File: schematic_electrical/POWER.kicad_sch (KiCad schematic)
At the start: 5 parts, among them SW1 WGCD_SPST_ILLUM_TOGGLE, SW2 WGCD_SPST_ILLUM_TOGGLE

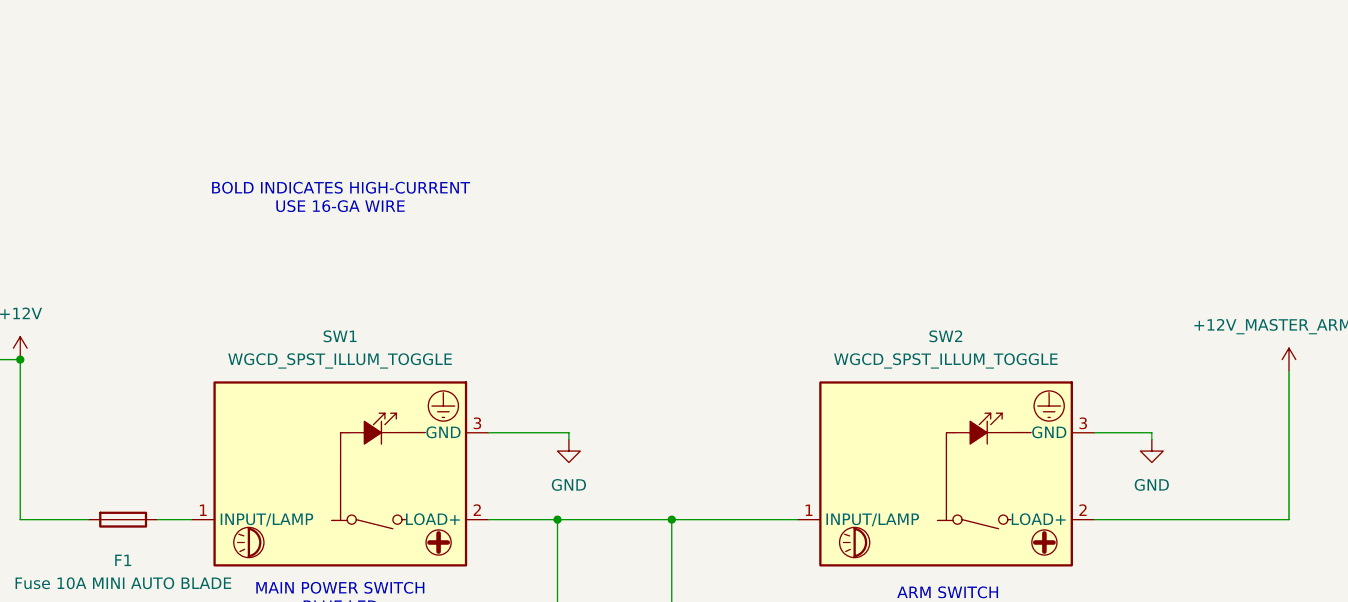
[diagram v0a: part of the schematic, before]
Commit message: Schematic options for bar placement bar box (button controller)
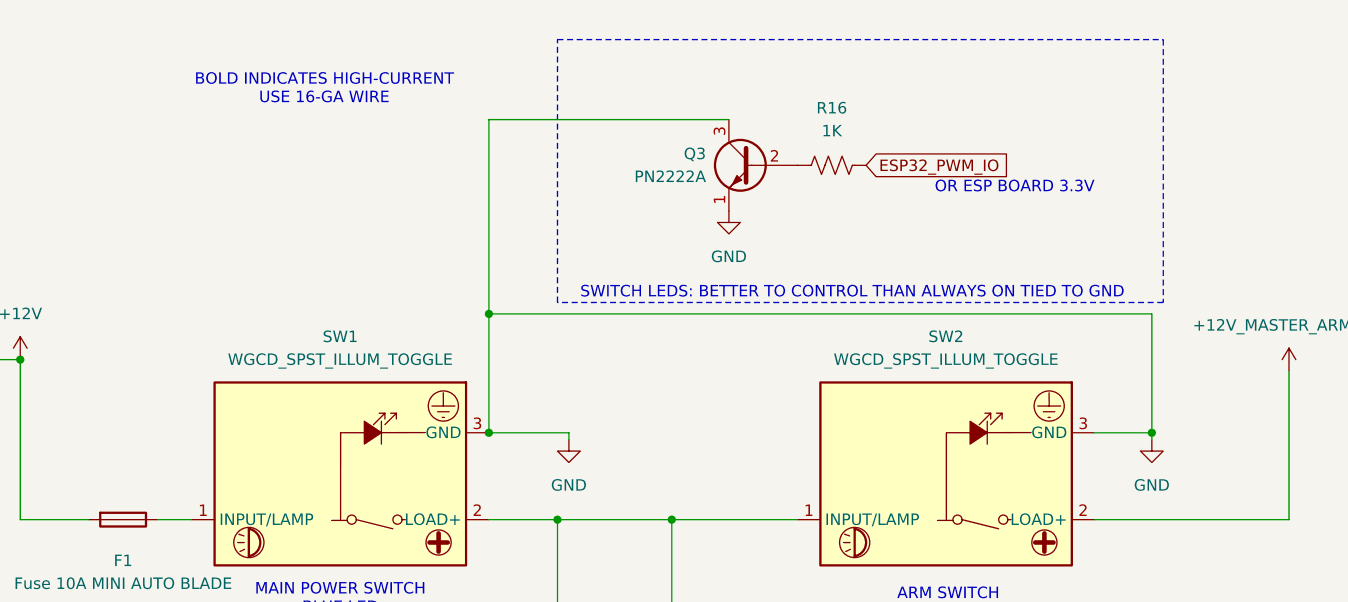
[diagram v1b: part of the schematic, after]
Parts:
- added Q3: PN2222A, Package_TO_SOT_THT:TO-92_Inline, symbol Transistor_BJT:PN2222A
- added R16: 1K, symbol Device:R_US
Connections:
- net GND: now also Q3.1 (E), Q3.3 (C)
- new net: Q3.2 (B), R16.1
- new net ESP32_PWM_IO: R16.2
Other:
- note added: "OR ESP BOARD 3.3V"
- note added: "SWITCH LEDS: BETTER TO CONTROL THAN ALWAYS ON TIED TO GND"

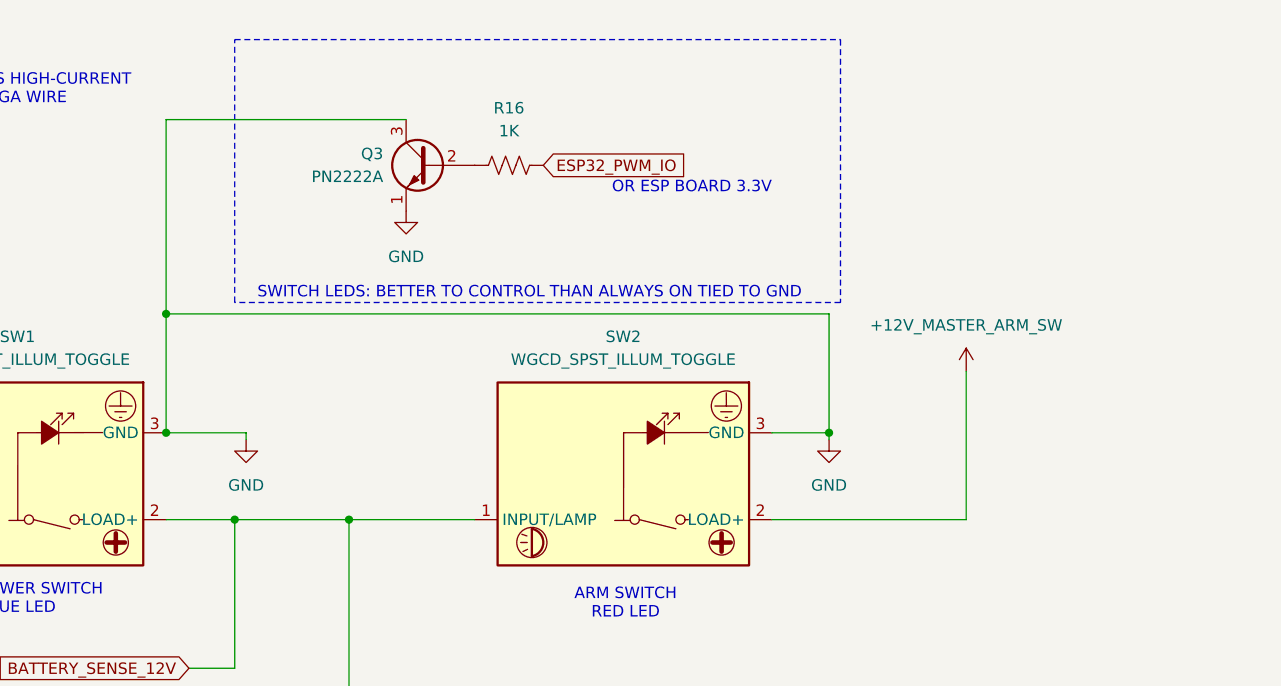
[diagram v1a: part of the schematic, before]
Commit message: Schematic for bar: use ULN2308 for button 12V lamps
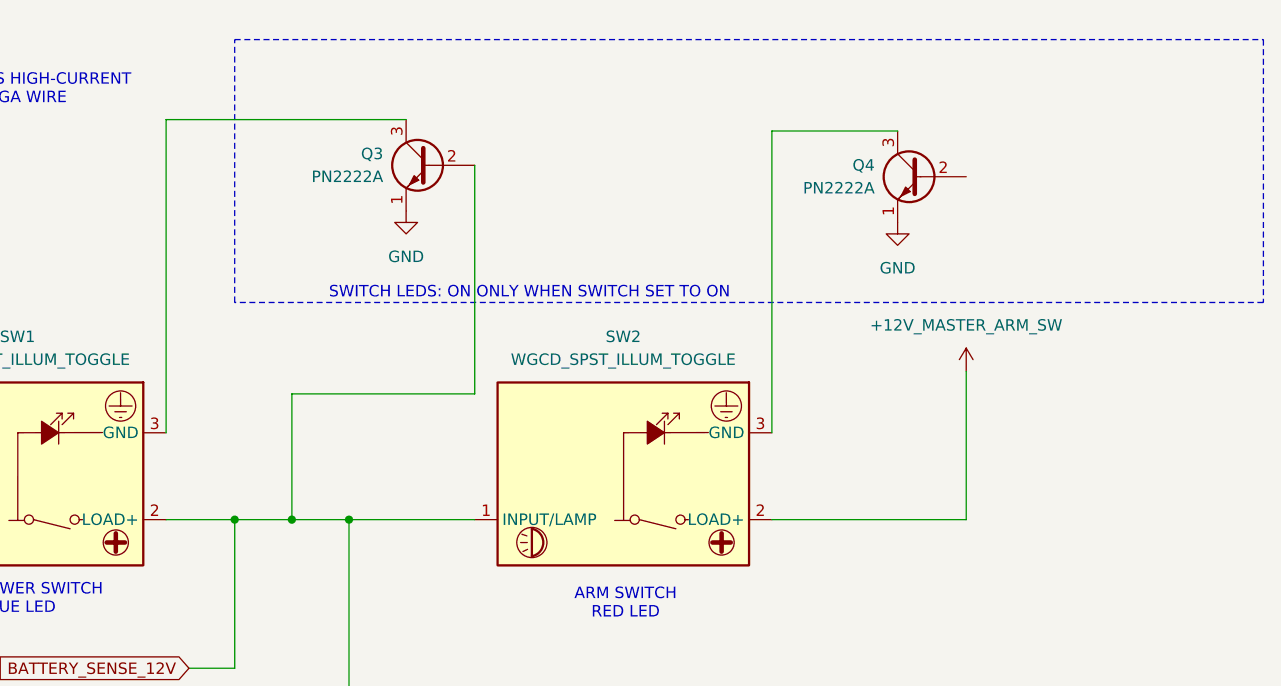
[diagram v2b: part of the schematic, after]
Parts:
- removed R16: 1K, symbol Device:R_US
- added Q4: PN2222A, Package_TO_SOT_THT:TO-92_Inline, symbol Transistor_BJT:PN2222A
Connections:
- net BATTERY_SENSE_12V: now also Q3.2 (B)
- net GND: now also Q4.1 (E); no longer Q3.3 (C), SW1.3 (GND), SW2.3 (GND)
- new net: Q3.3 (C), SW1.3 (GND)
- new net: Q4.3 (C), SW2.3 (GND)
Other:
- note added: "SWITCH LEDS: ON ONLY WHEN SWITCH SET TO ON"
- note removed: "OR ESP BOARD 3.3V"
- note removed: "SWITCH LEDS: BETTER TO CONTROL THAN ALWAYS ON TIED TO GND"

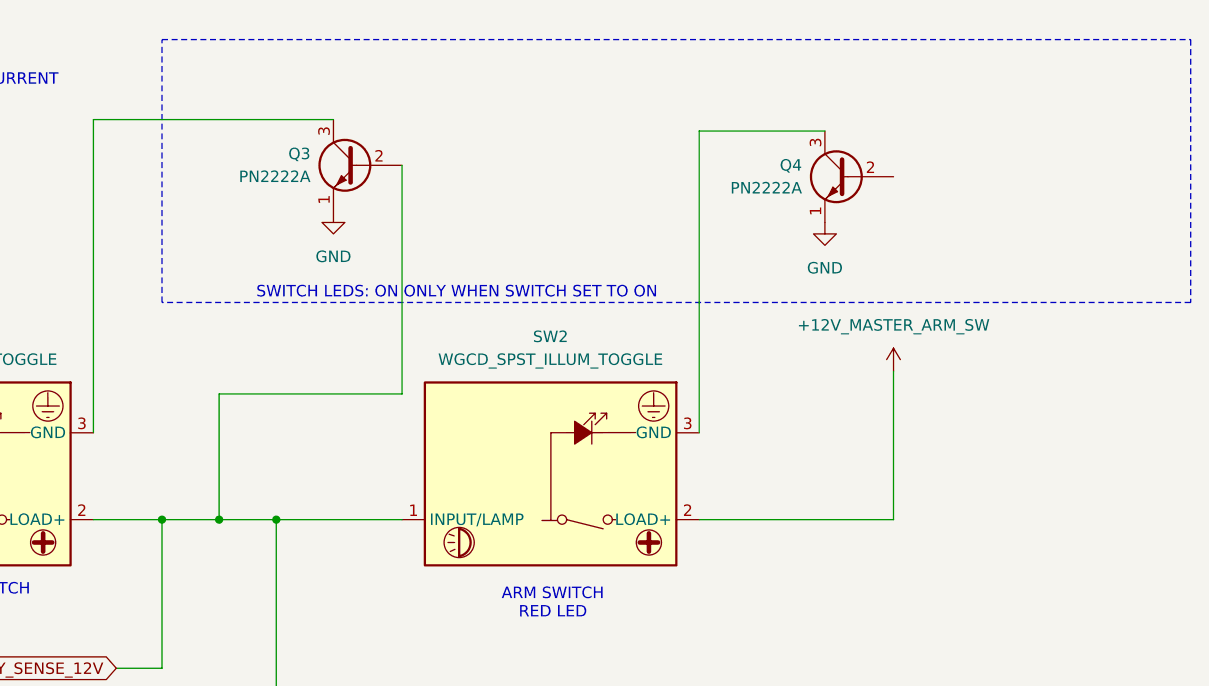
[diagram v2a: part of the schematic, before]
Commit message: Schematic as built for bar box. 12V fire enable switch wired in correct manner such that LED is off when switch is off.
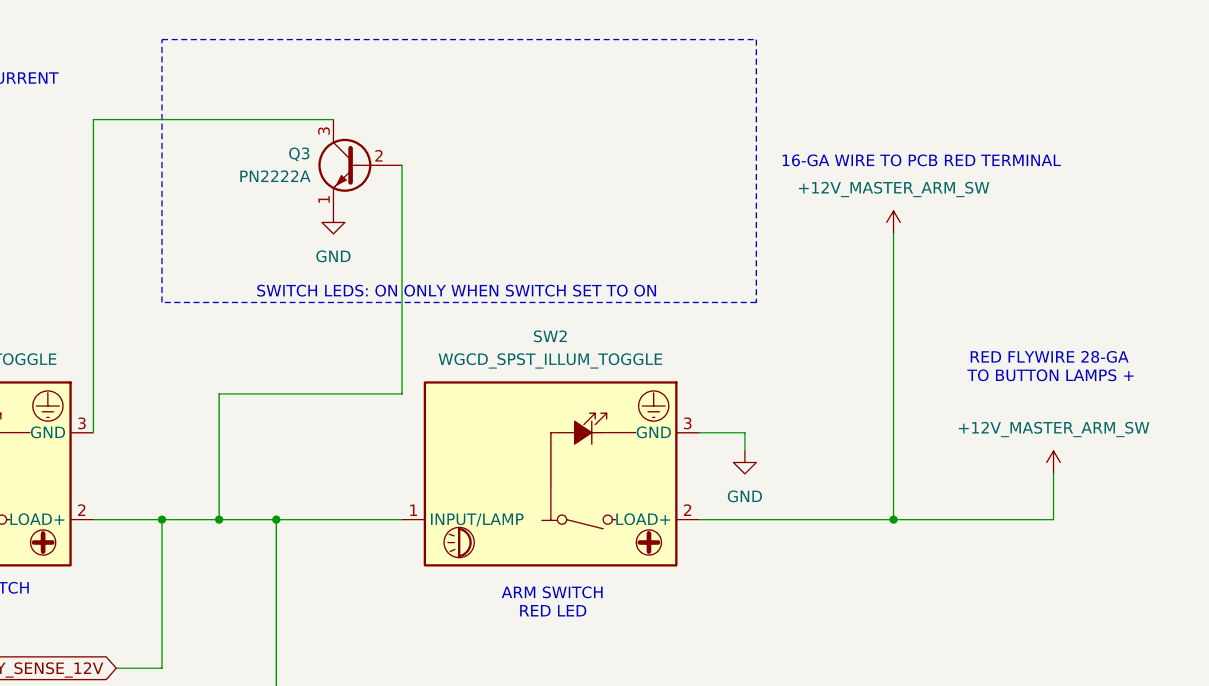
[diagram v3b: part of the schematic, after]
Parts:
- removed Q4: PN2222A, Package_TO_SOT_THT:TO-92_Inline, symbol Transistor_BJT:PN2222A
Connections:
- net GND: now also SW2.3 (GND)
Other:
- note added: "16-GA WIRE TO PCB RED TERMINAL"
- note added: "RED FLYWIRE 28-GA TO BUTTON LAMPS +"
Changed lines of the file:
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@@
+	)
+	(junction
+		(at 248.92 72.39)
+		(diameter 0)
+		(color 0 0 0 0)
 	)
 	(junction
@@
 	(wire
 		(pts
-			(xy 241.3 29.21) (xy 227.33 29.21)
-		)
-		(stroke
-			(width 0)
-			(type default)
-		)
-	)
-	(wire
-		(pts
 			(xy 173.99 58.42) (xy 194.31 58.42)
 		)
@@
 	(wire
 		(pts
-			(xy 248.92 72.39) (xy 248.92 55.88)
+			(xy 248.92 72.39) (xy 248.92 40.64)
 		)
 		(stroke
@@
 	(wire
 		(pts
+			(xy 232.41 64.77) (xy 232.41 62.738)
+		)
+		(stroke
+			(width 0)
+			(type default)
+		)
+	)
+	(wire
+		(pts
 			(xy 231.14 125.73) (xy 223.52 125.73)
 		)
@@
 	(wire
 		(pts
+			(xy 232.41 62.738) (xy 227.33 62.738)
+		)
+		(stroke
+			(width 0)
+			(type default)
+		)
+	)
+	(wire
+		(pts
 			(xy 180.34 72.39) (xy 194.31 72.39)
 		)
@@
 	(wire
 		(pts
+			(xy 266.7 72.39) (xy 248.92 72.39)
+		)
+		(stroke
+			(width 0)
+			(type default)
+		)
+	)
+	(wire
+		(pts
 			(xy 107.95 72.39) (xy 107.95 54.61)
 		)
@@
 	(wire
 		(pts
+			(xy 266.7 67.31) (xy 266.7 72.39)
+		)
+		(stroke
+			(width 0)
+			(type default)
+		)
+	)
+	(wire
+		(pts
 			(xy 160.02 27.94) (xy 160.02 62.738)
-		)
-		(stroke
-			(width 0)
-			(type default)
-		)
-	)
-	(wire
-		(pts
-			(xy 227.33 29.21) (xy 227.33 62.738)
 		)
 		(stroke
@@
 	(rectangle
 		(start 167.64 19.05)
-		(end 281.94 48.26)
+		(end 233.68 48.26)
 		(stroke
 			(width 0)
@@
 		)
 	)
+	(text "16-GA WIRE TO PCB RED TERMINAL"
+		(exclude_from_sim no)
+		(at 251.968 32.766 0)
+		(effects
+			(font
+				(size 1.27 1.27)
+			)
+		)
+	)
 	(text "FABRICATION NOTE: GND NODE WILL GANG\n16-GA FROM BATTERY-\n16-GA FROM DCDC-\n16-GA FROM DEUTCH 2-PIN- (EXT SUPPLY OPTION)\n16-GA FROM DEUTCH 3-PIN- (SOLENOID)\n2X 28-GA FROM TOGGLE LED GNDS\n1x 28-GA FROM PCB RED TERMINAL-"
 		(exclude_from_sim no)
@@
 		(exclude_from_sim no)
 		(at 215.646 139.446 0)
+		(effects
+			(font
+				(size 1.27 1.27)
+			)
+		)
+	)
+	(text "RED FLYWIRE 28-GA\n TO BUTTON LAMPS +"
+		(exclude_from_sim no)
+		(at 266.192 55.626 0)
 		(effects
 			(font
@@
 	(symbol
 		(lib_id "power:+12V")
-		(at 248.92 55.88 0)
+		(at 248.92 40.64 0)
 		(unit 1)
 		(exclude_from_sim no)
@@
 		(fields_autoplaced yes)
 		(property "Reference" "#PWR045"
-			(at 248.92 59.69 0)
+			(at 248.92 44.45 0)
 			(effects
 				(font
@@
 		)
 		(property "Value" "+12V_MASTER_ARM_SW"
-			(at 248.92 50.8 0)
+			(at 248.92 35.56 0)
 			(effects
 				(font
@@
 		)
 		(property "Footprint" ""
-			(at 248.92 55.88 0)
+			(at 248.92 40.64 0)
 			(effects
 				(font
@@
 		)
 		(property "Datasheet" ""
-			(at 248.92 55.88 0)
+			(at 248.92 40.64 0)
 			(effects
 				(font
@@
 		)
 		(property "Description" "Power symbol creates a global label with name \"+12V\""
-			(at 248.92 55.88 0)
+			(at 248.92 40.64 0)
 			(effects
 				(font
@@
 				(path "/f3653ac0-a28a-4ee8-bcf5-236139001455/6657731a-46b5-42dc-8611-bac46a2b6e5c"
 					(reference "#PWR045")
-					(unit 1)
-				)
-			)
-		)
-	)
-	(symbol
-		(lib_id "Transistor_BJT:PN2222A")
-		(at 243.84 34.29 0)
-		(mirror y)
-		(unit 1)
-		(exclude_from_sim no)
-		(in_bom yes)
-		(on_board yes)
-		(dnp no)
-		(property "Reference" "Q4"
-			(at 238.76 33.0199 0)
-			(effects
-				(font
-					(size 1.27 1.27)
-				)
-				(justify left)
-			)
-		)
-		(property "Value" "PN2222A"
-			(at 238.76 35.5599 0)
-			(effects
-				(font
-					(size 1.27 1.27)
-				)
-				(justify left)
-			)
-		)
-		(property "Footprint" "Package_TO_SOT_THT:TO-92_Inline"
-			(at 238.76 36.195 0)
-			(effects
-				(font
-					(size 1.27 1.27)
-					(italic yes)
-				)
-				(justify left)
-				(hide yes)
-			)
-		)
-		(property "Datasheet" "https://www.onsemi.com/pub/Collateral/PN2222-D.PDF"
-			(at 243.84 34.29 0)
-			(effects
-				(font
-					(size 1.27 1.27)
-				)
-				(justify left)
-				(hide yes)
-			)
-		)
-		(property "Description" "1A Ic, 40V Vce, NPN Transistor, General Purpose Transistor, TO-92"
-			(at 243.84 34.29 0)
-			(effects
-				(font
-					(size 1.27 1.27)
-				)
-				(hide yes)
-			)
-		)
-		(pin "1"
-		)
-		(pin "2"
-		)
-		(pin "3"
-		)
-		(instances
-			(project "pylons_boosh_remote_reciver"
-				(path "/f3653ac0-a28a-4ee8-bcf5-236139001455/6657731a-46b5-42dc-8611-bac46a2b6e5c"
-					(reference "Q4")
 					(unit 1)
 				)
@@
 	(symbol
 		(lib_id "power:GND")
+		(at 232.41 64.77 0)
+		(unit 1)
+		(exclude_from_sim no)
+		(in_bom yes)
+		(on_board yes)
+		(dnp no)
+		(fields_autoplaced yes)
+		(property "Reference" "#PWR024"
+			(at 232.41 71.12 0)
+			(effects
+				(font
+					(size 1.27 1.27)
+				)
+				(hide yes)
+			)
+		)
+		(property "Value" "GND"
+			(at 232.41 69.85 0)
+			(effects
+				(font
+					(size 1.27 1.27)
+				)
+			)
+		)
+		(property "Footprint" ""
+			(at 232.41 64.77 0)
+			(effects
+				(font
+					(size 1.27 1.27)
+				)
+				(hide yes)
+			)
+		)
+		(property "Datasheet" ""
+			(at 232.41 64.77 0)
+			(effects
+				(font
+					(size 1.27 1.27)
+				)
+				(hide yes)
+			)
+		)
+		(property "Description" "Power symbol creates a global label with name \"GND\" , ground"
+			(at 232.41 64.77 0)
+			(effects
+				(font
+					(size 1.27 1.27)
+				)
+				(hide yes)
+			)
+		)
+		(pin "1"
+		)
+		(instances
+			(project "pylons_boosh_remote_reciver"
+				(path "/f3653ac0-a28a-4ee8-bcf5-236139001455/6657731a-46b5-42dc-8611-bac46a2b6e5c"
+					(reference "#PWR024")
+					(unit 1)
+				)
+			)
+		)
+	)
+	(symbol
+		(lib_id "power:+12V")
+		(at 266.7 67.31 0)
+		(unit 1)
+		(exclude_from_sim no)
+		(in_bom yes)
+		(on_board yes)
+		(dnp no)
+		(fields_autoplaced yes)
+		(property "Reference" "#PWR014"
+			(at 266.7 71.12 0)
+			(effects
+				(font
+					(size 1.27 1.27)
+				)
+				(hide yes)
+			)
+		)
+		(property "Value" "+12V_MASTER_ARM_SW"
+			(at 266.7 62.23 0)
+			(effects
+				(font
+					(size 1.27 1.27)
+				)
+			)
+		)
+		(property "Footprint" ""
+			(at 266.7 67.31 0)
+			(effects
+				(font
+					(size 1.27 1.27)
+				)
+				(hide yes)
+			)
+		)
+		(property "Datasheet" ""
+			(at 266.7 67.31 0)
+			(effects
+				(font
+					(size 1.27 1.27)
+				)
+				(hide yes)
+			)
+		)
+		(property "Description" "Power symbol creates a global label with name \"+12V\""
+			(at 266.7 67.31 0)
+			(effects
+				(font
+					(size 1.27 1.27)
+				)
+				(hide yes)
+			)
+		)
+		(pin "1"
+		)
+		(instances
+			(project "pylons_boosh_remote_reciver"
+				(path "/f3653ac0-a28a-4ee8-bcf5-236139001455/6657731a-46b5-42dc-8611-bac46a2b6e5c"
+					(reference "#PWR014")
+					(unit 1)
+				)
+			)
+		)
+	)
+	(symbol
+		(lib_id "power:GND")
 		(at 186.69 38.1 0)
 		(unit 1)
@@
 					(unit 1)
 				)
-			)
-		)
-	)
-	(symbol
-		(lib_id "power:GND")
-		(at 241.3 39.37 0)
-		(unit 1)
-		(exclude_from_sim no)
-		(in_bom yes)
-		(on_board yes)
-		(dnp no)
-		(fields_autoplaced yes)
-		(property "Reference" "#PWR014"
-			(at 241.3 45.72 0)
-			(effects
-				(font
-					(size 1.27 1.27)
-				)
-				(hide yes)
-			)
-		)
-		(property "Value" "GND"
-			(at 241.3 44.45 0)
-			(effects
-				(font
-					(size 1.27 1.27)
-				)
-			)
-		)
-		(property "Footprint" ""
-			(at 241.3 39.37 0)
-			(effects
-				(font
-					(size 1.27 1.27)
-				)
-				(hide yes)
-			)
-		)
-		(property "Datasheet" ""
-			(at 241.3 39.37 0)
-			(effects
-				(font
-					(size 1.27 1.27)
-				)
-				(hide yes)
-			)
-		)
-		(property "Description" "Power symbol creates a global label with name \"GND\" , ground"
-			(at 241.3 39.37 0)
-			(effects
-				(font
-					(size 1.27 1.27)
-				)
-				(hide yes)
-			)
-		)
-		(pin "1"
-		)
-		(instances
-			(project "pylons_boosh_remote_reciver"
-				(path "/f3653ac0-a28a-4ee8-bcf5-236139001455/6657731a-46b5-42dc-8611-bac46a2b6e5c"
-					(reference "#PWR014")
-					(unit 1)
-				)
